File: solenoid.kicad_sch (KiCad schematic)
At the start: 10 parts, among them J7 Solenoid, Q10 DMG3402L

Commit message: Addressed comments; See issue for notes
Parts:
- R77: Manufacturer Generic -> Stackpole Electronics Inc; Part # Generic RES SMD 0.1 OHM 0.1% 2W 2512 -> CSRN2512FTR100
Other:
- note removed: "find part"
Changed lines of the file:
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@@
-		)
-	)
-	(text "find part"
-		(exclude_from_sim no)
-		(at 147.32 110.998 0)
-		(effects
-			(font
-				(size 1.27 1.27)
-				(color 255 32 32 1)
-			)
 		)
 	)
@@
 			)
 		)
-		(property "Description" "FIND SPEWfUAF"
+		(property "Description" ""
 			(at 139.7 106.68 0)
 			(effects
@@
 			)
 		)
-		(property "Manufacturer" "Generic"
+		(property "Manufacturer" " Stackpole Electronics Inc"
 			(at 139.7 106.68 0)
 			(effects
@@
 			)
 		)
-		(property "Part #" "Generic RES SMD 0.1 OHM 0.1% 2W 2512"
+		(property "Part #" "CSRN2512FTR100"
 			(at 139.7 106.68 0)
 			(effects

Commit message: Added power sense to rocket2-battery with voltage follower, added +1 solenoids and PT circuit, made new gx connectors
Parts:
- J7: footprint Connector_PinHeader_2.54mm:PinHeader_1x03_P2.54mm_Vertical -> 0UCIRP-KiCAD-Lib:GX-16 3 pin

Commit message: version in PCBway 12/12/2025
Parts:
- J7: now not fitted
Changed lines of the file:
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@@
 		(in_bom yes)
 		(on_board yes)
-		(dnp no)
+		(dnp yes)
 		(property "Reference" "J7"
 			(at 116.84 80.01 0)

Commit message: added some production files
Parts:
- D23: Part # SDT8A100P5-7 -> SBR10E45P5-13
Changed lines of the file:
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@@
 			)
 		)
-		(property "Datasheet" "https://www.diodes.com/assets/Datasheets/SDT8A100P5.pdf"
+		(property "Datasheet" "https://www.diodes.com/assets/Datasheets/SBR10E45P5.pdf"
 			(at 151.13 81.28 90)
 			(effects
@@
 			)
 		)
-		(property "Part #" "SDT8A100P5-7"
+		(property "Part #" "SBR10E45P5-13"
 			(at 151.13 81.28 0)
 			(effects

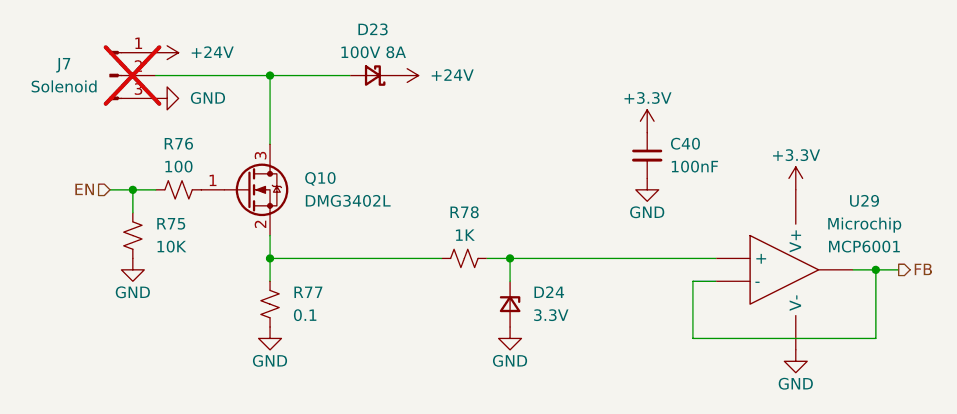
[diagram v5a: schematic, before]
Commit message: changed charging circuit for Insta360, gonna send in now on JLCPCB
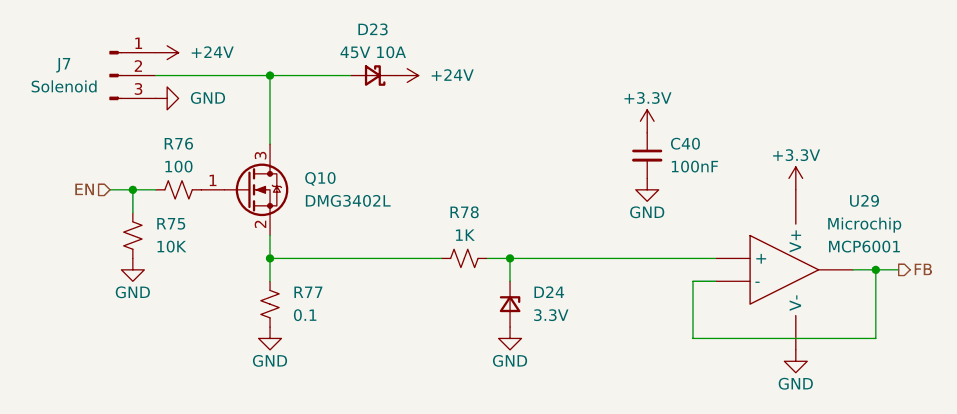
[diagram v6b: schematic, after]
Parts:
- D23: value 100V 8A -> 45V 10A
- J7: now fitted
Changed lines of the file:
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@@
 			)
 		)
-		(property "Description" ""
+		(property "Description" "Resistor, small US symbol"
 			(at 139.7 106.68 0)
 			(effects
@@
 			)
 		)
-		(property "Description" ""
+		(property "Description" "Power symbol creates a global label with name \"GND\" , ground"
 			(at 124.46 101.6 0)
 			(effects
@@
 			)
 		)
-		(property "Description" ""
+		(property "Description" "Power symbol creates a global label with name \"+3.3V\""
 			(at 181.61 87.63 0)
 			(effects
@@
 			)
 		)
-		(property "Description" ""
+		(property "Description" "Power symbol creates a global label with name \"GND\" , ground"
 			(at 166.37 109.22 0)
 			(effects
@@
 			)
 		)
-		(property "Description" ""
+		(property "Description" "Power symbol creates a global label with name \"GND\" , ground"
 			(at 198.12 111.76 0)
 			(effects
@@
 			)
 		)
-		(property "Datasheet" "https://www.onsemi.com/pdf/datasheet/mmsz4678t1-d.pdf"
+		(property "Datasheet" "~"
 			(at 166.37 106.68 90)
 			(effects
@@
 			)
 		)
-		(property "Description" ""
+		(property "Description" "Zener diode, small symbol"
 			(at 166.37 106.68 0)
 			(effects
@@
 			)
 		)
-		(property "Description" ""
+		(property "Description" "Power symbol creates a global label with name \"GND\" , ground"
 			(at 127 83.82 0)
 			(effects
@@
 			)
 		)
-		(property "Description" ""
+		(property "Description" "Power symbol creates a global label with name \"GND\" , ground"
 			(at 139.7 109.22 0)
 			(effects
@@
 			)
 		)
-		(property "Description" ""
+		(property "Description" "Power symbol creates a global label with name \"GND\" , ground"
 			(at 181.61 92.71 0)
 			(effects
@@
 			)
 		)
-		(property "Description" ""
+		(property "Description" "Unpolarized capacitor, small symbol"
 			(at 181.61 90.17 0)
 			(effects
@@
 			)
 		)
-		(property "Description" ""
+		(property "Description" "Power symbol creates a global label with name \"+24V\""
 			(at 127 78.74 0)
 			(effects
@@
 		(in_bom yes)
 		(on_board yes)
-		(dnp yes)
+		(dnp no)
 		(property "Reference" "J7"
 			(at 116.84 80.01 0)
@@
 			)
 		)
-		(property "Description" ""
+		(property "Description" "Generic connector, single row, 01x03, script generated"
 			(at 121.92 81.28 0)
 			(effects
@@
 			)
 		)
-		(property "Description" ""
+		(property "Description" "Resistor, small US symbol"
 			(at 124.46 99.06 0)
 			(effects
@@
 			)
 		)
-		(property "Description" ""
+		(property "Description" "Power symbol creates a global label with name \"+24V\""
 			(at 153.67 81.28 0)
 			(effects
@@
 			)
 		)
-		(property "Value" "100V 8A"
+		(property "Value" "45V 10A"
 			(at 151.13 78.74 0)
 			(effects
@@
 			)
 		)
-		(property "Datasheet" "https://www.diodes.com/assets/Datasheets/SBR10E45P5.pdf"
+		(property "Datasheet" "~"
 			(at 151.13 81.28 90)
 			(effects
@@
 			)
 		)
-		(property "Description" ""
+		(property "Description" "Schottky diode, small symbol"
 			(at 151.13 81.28 0)
 			(effects
@@
 			)
 		)
-		(property "Description" ""
+		(property "Description" "Power symbol creates a global label with name \"+3.3V\""
 			(at 198.12 93.98 0)
 			(effects
@@
 			)
 		)
-		(property "Description" ""
+		(property "Description" "Resistor, small US symbol"
 			(at 161.29 101.6 0)
 			(effects
@@
 			)
 		)
-		(property "Description" ""
+		(property "Description" "Resistor, small US symbol"
 			(at 129.54 93.98 0)
 			(effects
